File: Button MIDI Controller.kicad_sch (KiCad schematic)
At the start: 33 parts, among them J1 SWD, J2 USB_C_Receptacle_USB2.0_16P, U1 RP2040, U2 W25Q16JVZPIQ, U3 USBLC6-2SC6, U4 XC6206PxxxMR, Y1 X322512MSB4SI

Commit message: updates
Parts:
- C1, C10, C11, C12, C13, C14, C15, C16, C17, C2, C3, C4, C5, C6, C7, C8, C9: footprint Capacitor_SMD:C_0603_1608Metric -> Capacitor_SMD:C_0402_1005Metric-notxt
- F1: footprint Fuse:Fuse_0603_1608Metric -> Fuse:Fuse_0402_1005Metric-notxt
- J1: footprint Connector_PinHeader_1.00mm:PinHeader_1x05_P1.00mm_Vertical_SMD_Pin1Right -> Connector_PinHeader_1.00mm:PinHeader_1x05_P1.00mm_Vertical_SMD_Pin1Right-notxt
- J2: footprint Connector_USB:USB_C_Receptacle_G-Switch_GT-USB-7025 -> Connector_USB:USB_C_Receptacle_G-Switch_GT-USB-7025-notxt
- R1, R2, R3, R4, R5, R6, R7: footprint Resistor_SMD:R_0603_1608Metric -> Resistor_SMD:R_0402_1005Metric-notext
- TP1: footprint TestPoint:TestPoint_Pad_4.0x4.0mm -> TestPoint:TestPoint_Pad_1.0x1.0mm-notxt
- U1: footprint Footprints:RP2040-QFN-56 -> Footprints:RP2040-QFN-56-notext
- U2: footprint W25Q16JVZPIQ:SON127P500X600X80-9N -> W25Q16JVZPIQ:SON127P500X600X80-9N-notxt
- U3: footprint Package_TO_SOT_SMD:SOT-23-6 -> Package_TO_SOT_SMD:SOT-23-6-notxt
- U4: footprint Package_TO_SOT_SMD:SOT-23-3 -> Package_TO_SOT_SMD:SOT-23-3-notxt
- Y1: footprint Crystal:Crystal_SMD_7050-4Pin_7.0x5.0mm -> Crystal:Crystal_SMD_2016-4Pin_2.0x1.6mm-notxt
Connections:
- net COL2: now reaches U1.11 (GPIO8)
- net COL1: now reaches U1.12 (GPIO9)
- net COL0: now reaches U1.13 (GPIO10)
- net COL8: now reaches U1.14 (GPIO11)
- net COL7: now reaches U1.17 (GPIO14)
- net COL6: now reaches U1.18 (GPIO15)
- net LED_DIN: now reaches U1.2 (GPIO0)
- net ROW0: now reaches U1.27 (GPIO16)
- net COL5: now reaches U1.28 (GPIO17)
- net ROW7: now reaches U1.3 (GPIO1)
- net COL4: now reaches U1.34 (GPIO22)
- net COL3: now reaches U1.35 (GPIO23)
- net ROW6: now reaches U1.4 (GPIO2)
- net ROW5: now reaches U1.5 (GPIO3)
- net ROW4: now reaches U1.6 (GPIO4)
- net ROW3: now reaches U1.7 (GPIO5)
- net ROW2: now reaches U1.8 (GPIO6)
- net ROW1: now reaches U1.9 (GPIO7)
- no-connect marks 2 -> 14

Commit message: yeah have some updates my g
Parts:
- C1, C2: JLCPCB Part (none) -> C541361
- C10, C11, C12, C13, C14, C15, C3, C7, C8, C9: JLCPCB Part (none) -> C541407
- C16, C4, C5, C6: JLCPCB Part (none) -> C437522
- C17: JLCPCB Part (none) -> C6119763
- F1: JLCPCB Part (none) -> C136320
- J1, TP1: now left out of the parts list
- J2: JLCPCB Part (none) -> C963213
- R1, R2, R5: JLCPCB Part (none) -> C11702
- R3, R4: JLCPCB Part (none) -> C25100
- R6, R7: JLCPCB Part (none) -> C25905
- U1: JLCPCB Part (none) -> C2040
- U2: JLCPCB Part (none) -> C377853
- U3: JLCPCB Part (none) -> C7519
- U4: JLCPCB Part (none) -> C5148692
- Y1: JLCPCB Part (none) -> C9002

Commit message: updates
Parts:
- F1: footprint Fuse:Fuse_0402_1005Metric-notxt -> Fuse:Fuse_1206_3216Metric
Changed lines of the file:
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@@
 			)
 		)
-		(property "Footprint" "Fuse:Fuse_0402_1005Metric-notxt"
+		(property "Footprint" "Fuse:Fuse_1206_3216Metric"
 			(at 199.39 113.03 0)
 			(effects

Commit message: boardstar updates & me ruining it
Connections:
- net COL0: now also U1.34 (GPIO22); no longer U1.13 (GPIO10)
- net COL1: now also U1.35 (GPIO23); no longer U1.12 (GPIO9)
- net COL2: now also U1.36 (GPIO24); no longer U1.11 (GPIO8)
- net COL3: now also U1.37 (GPIO25); no longer U1.35 (GPIO23)
- net COL4: now also U1.41 (GPIO29/ADC3); no longer U1.34 (GPIO22)
- net COL5: now also U1.40 (GPIO28/ADC2); no longer U1.28 (GPIO17)
- net COL6: now also U1.39 (GPIO27/ADC1); no longer U1.18 (GPIO15)
- net COL7: now also U1.38 (GPIO26/ADC0); no longer U1.17 (GPIO14)
- net COL8: now also U1.29 (GPIO18); no longer U1.14 (GPIO11)
- net ROW0: now also U1.5 (GPIO3); no longer U1.27 (GPIO16)
- net ROW1: now also U1.7 (GPIO5); no longer U1.9 (GPIO7)
- net ROW2: now also U1.14 (GPIO11); no longer U1.8 (GPIO6)
- net ROW3: now also U1.8 (GPIO6); no longer U1.7 (GPIO5)
- net ROW4: now also U1.9 (GPIO7); no longer U1.6 (GPIO4)
- net ROW5: now also U1.11 (GPIO8); no longer U1.5 (GPIO3)
- net ROW6: now also U1.12 (GPIO9); no longer U1.4 (GPIO2)
- net ROW7: now also U1.13 (GPIO10); no longer U1.3 (GPIO1)

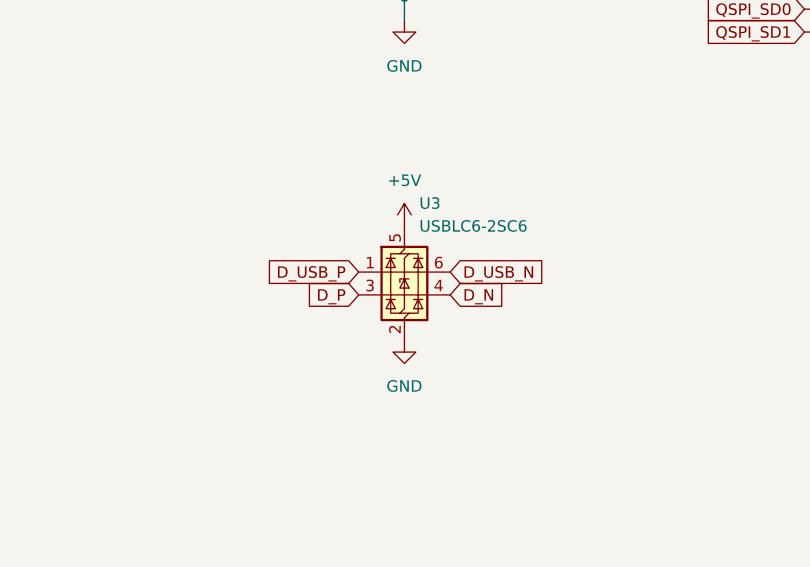
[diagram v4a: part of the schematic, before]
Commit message: reroute usb, crystal, usblc
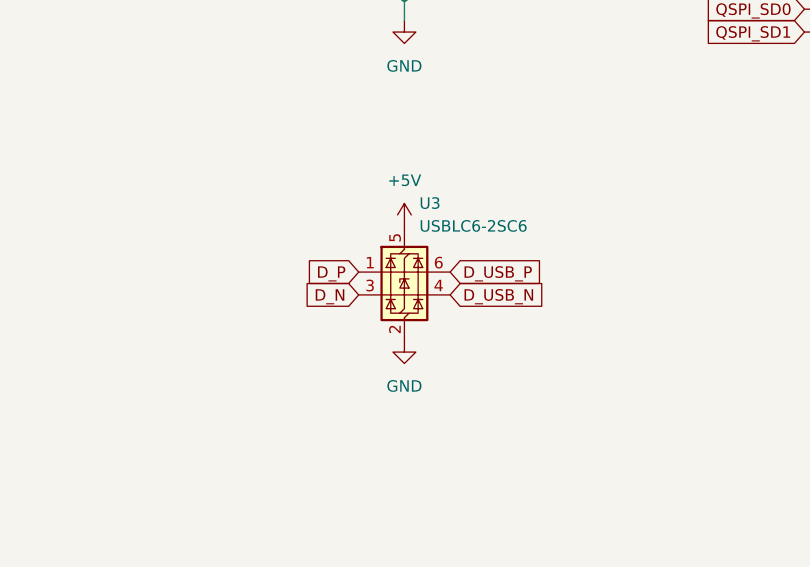
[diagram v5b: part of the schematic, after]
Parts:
- Y1: footprint Crystal:Crystal_SMD_2016-4Pin_2.0x1.6mm-notxt -> Crystal:Crystal_SMD_3225-4Pin_3.2x2.5mm
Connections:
- net D_N: now also U3.3 (I/O2); no longer U3.4 (I/O2)
- net D_P: now also U3.1 (I/O1); no longer U3.3 (I/O2)
- net D_USB_N: now also U3.4 (I/O2); no longer U3.6 (I/O1)
- net D_USB_P: now also U3.6 (I/O1); no longer U3.1 (I/O1)
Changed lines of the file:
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@@
 	(global_label "D_USB_N"
 		(shape input)
-		(at 176.53 71.12 0)
+		(at 176.53 73.66 0)
 		(fields_autoplaced yes)
 		(effects
@@
 		)
 		(property "Intersheetrefs" "${INTERSHEET_REFS}"
-			(at 187.8609 71.12 0)
+			(at 187.8609 73.66 0)
 			(effects
 				(font
@@
 	(global_label "D_P"
 		(shape input)
-		(at 166.37 73.66 180)
+		(at 166.37 71.12 180)
 		(fields_autoplaced yes)
 		(effects
@@
 		)
 		(property "Intersheetrefs" "${INTERSHEET_REFS}"
-			(at 159.8772 73.66 0)
+			(at 159.8772 71.12 0)
 			(effects
 				(font
@@
 	(global_label "D_USB_P"
 		(shape input)
-		(at 166.37 71.12 180)
+		(at 176.53 71.12 0)
 		(fields_autoplaced yes)
 		(effects
@@
 				(size 1.27 1.27)
 			)
-			(justify right)
+			(justify left)
 		)
 		(property "Intersheetrefs" "${INTERSHEET_REFS}"
-			(at 155.0996 71.12 0)
+			(at 187.8004 71.12 0)
 			(effects
 				(font
 					(size 1.27 1.27)
 				)
-				(justify right)
+				(justify left)
 				(hide yes)
 			)
@@
 	(global_label "D_N"
 		(shape input)
-		(at 176.53 73.66 0)
+		(at 166.37 73.66 180)
 		(fields_autoplaced yes)
 		(effects
@@
 				(size 1.27 1.27)
 			)
-			(justify left)
+			(justify right)
 		)
 		(property "Intersheetrefs" "${INTERSHEET_REFS}"
-			(at 183.0833 73.66 0)
+			(at 159.8167 73.66 0)
 			(effects
 				(font
 					(size 1.27 1.27)
 				)
-				(justify left)
+				(justify right)
 				(hide yes)
 			)
@@
 			)
 		)
-		(property "Footprint" "Crystal:Crystal_SMD_2016-4Pin_2.0x1.6mm-notxt"
+		(property "Footprint" "Crystal:Crystal_SMD_3225-4Pin_3.2x2.5mm"
 			(at 237.49 78.74 0)
 			(effects
